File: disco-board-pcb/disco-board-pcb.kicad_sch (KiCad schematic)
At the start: 140 parts, among them J1 Conn_02x32_Odd_Even, J2 Conn_02x32_Odd_Even, U1 MMA8653FCR1

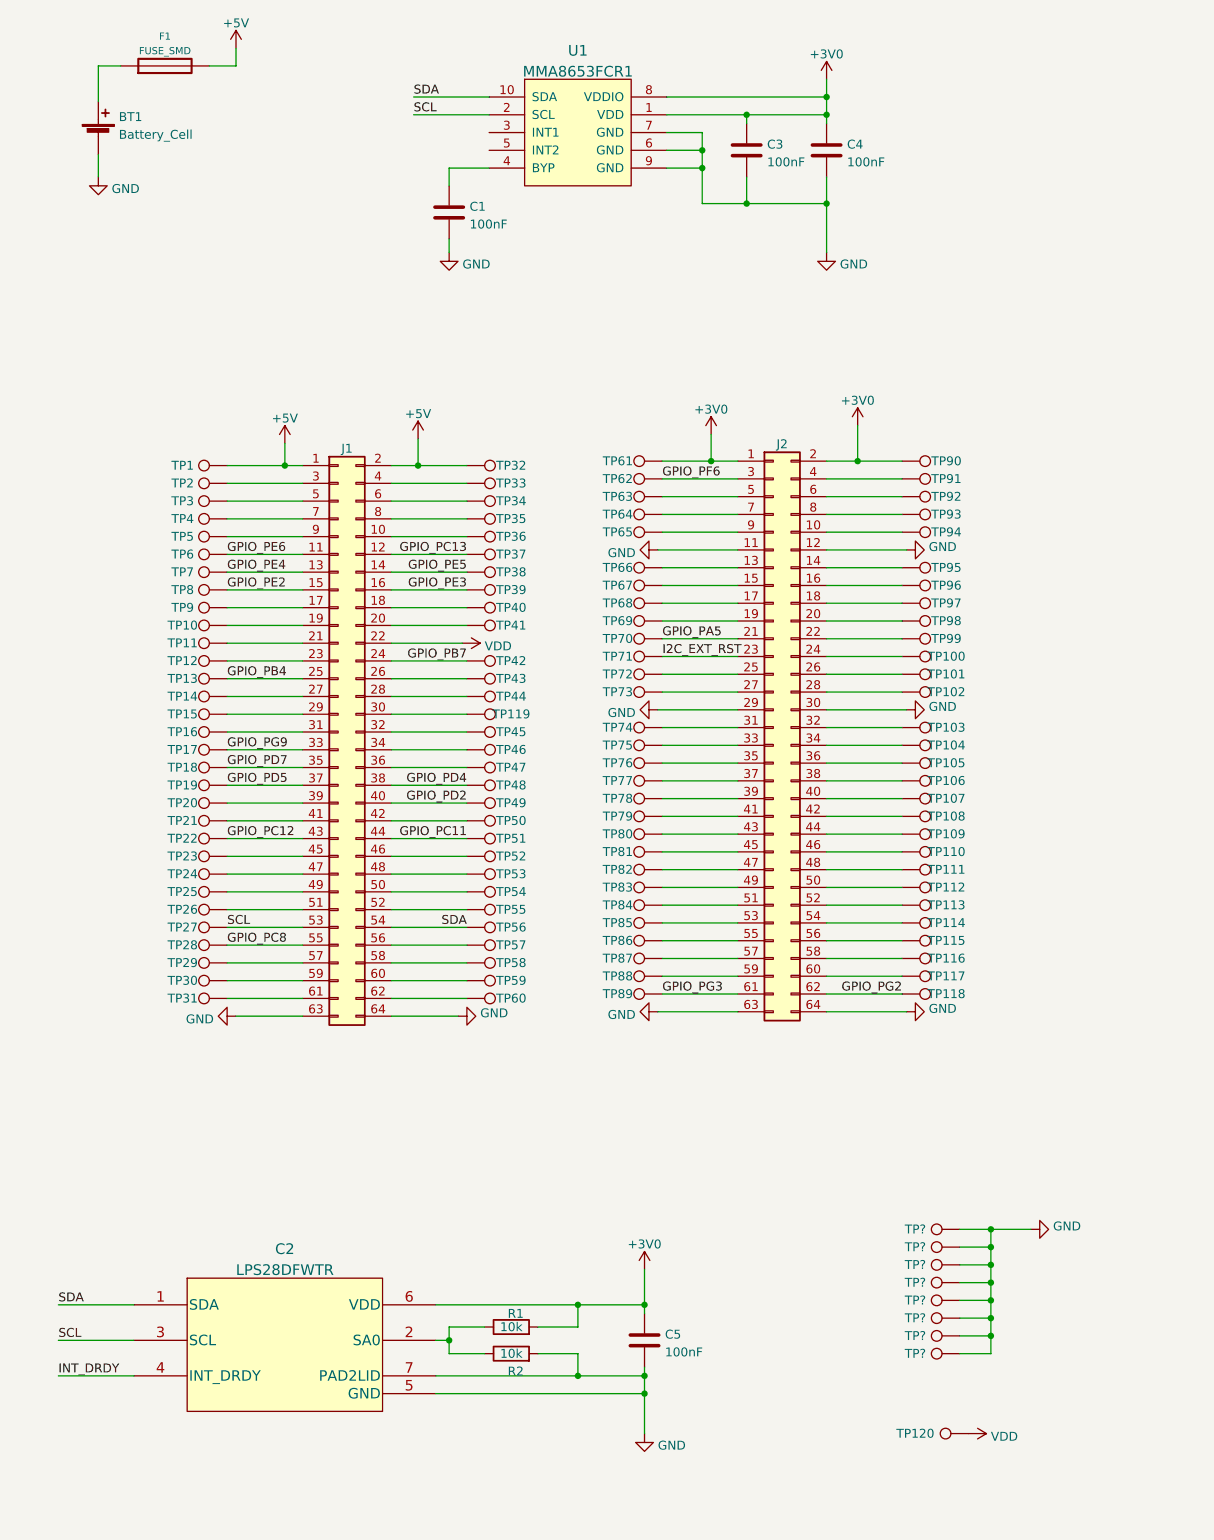
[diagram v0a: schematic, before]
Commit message: Completed routing the board
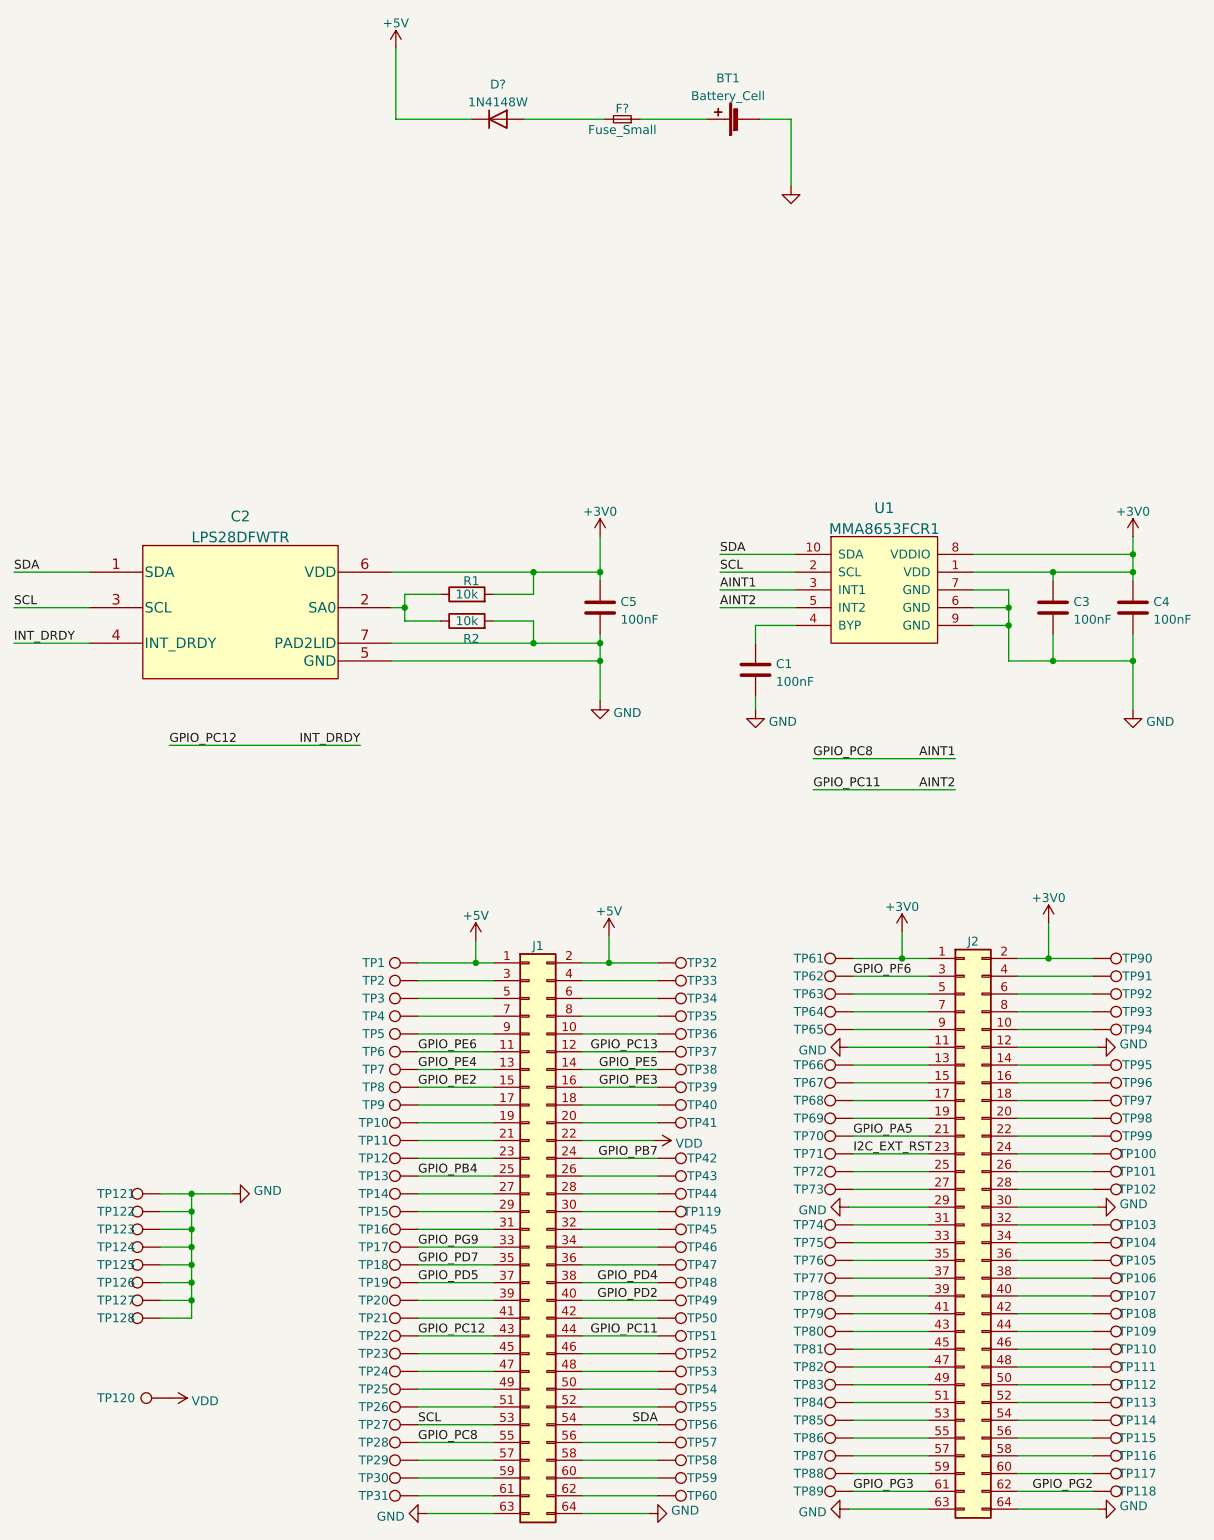
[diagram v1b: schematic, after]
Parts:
- removed F1: FUSE_SMD, Fuse_AKL:Fuse_1206_3216Metric_Pad1.42x1.75mm_BigPads, symbol Special-local:FUSE_SMD
- added D?: 1N4148W, Diode_SMD:D_SOD-123, symbol Diode:1N4148W
- added F?: Fuse_Small, Fuse_AKL:Fuse_1206_3216Metric, symbol magniblu-rescue:Fuse_Small
- gave numbers to parts that had none: 8
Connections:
- net GPIO_PC11 is gone; now on net AINT2: J1.44 (Pin_44), TP51.1
- net GPIO_PC8 is gone; now on net AINT1: J1.55 (Pin_55), TP28.1
- net INT_DRDY is gone; now on net GPIO_PC12: C2.4 (INT_DRDY)
- net +5V: now also D?.1 (K)
- net at BT1.1 (+): now also F?.1
- net AINT1: now reaches U1.3 (INT1)
- net AINT2: now reaches U1.5 (INT2)
- new net: D?.2 (A), F?.2
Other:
- moved on the sheet: BT1, C1, C2, C3, C4, C5, J1, J2, R1, R2, TP1, TP10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

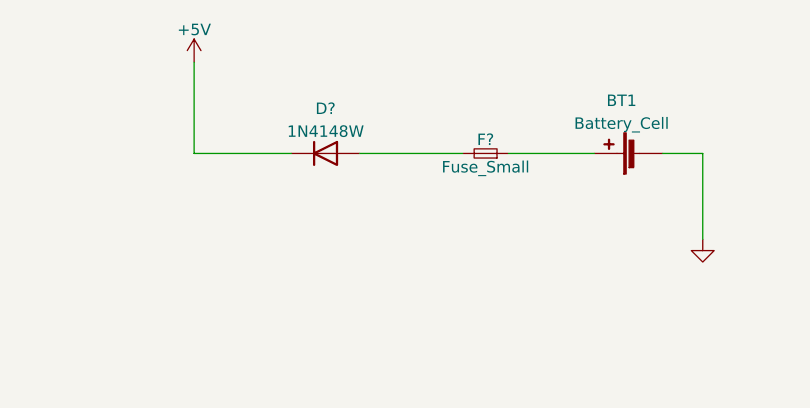
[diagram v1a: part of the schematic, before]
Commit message: Adding gerbers and completing saving schematic
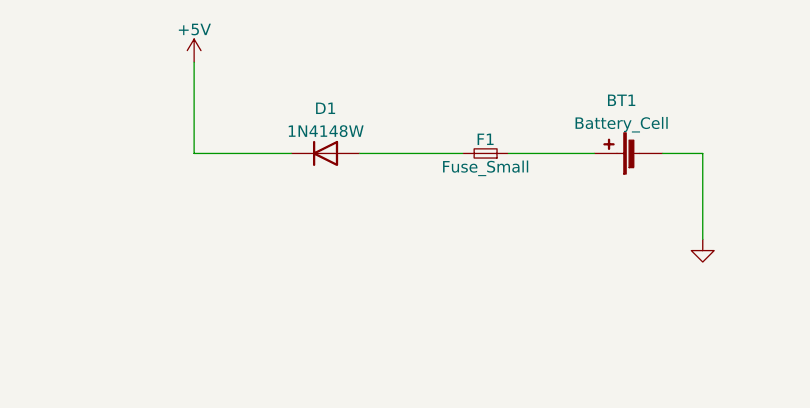
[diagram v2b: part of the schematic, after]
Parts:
- gave numbers to parts that had none: 2
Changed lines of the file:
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@@
   (symbol (lib_id "magniblu-rescue:Fuse_Small") (at 108.585 45.085 180) (unit 1)
     (in_bom yes) (on_board yes)
-    (property "Reference" "F?" (id 0) (at 108.585 43.561 0))
+    (property "Reference" "F1" (id 0) (at 108.585 43.561 0))
     (property "Value" "Fuse_Small" (id 1) (at 108.585 46.609 0))
     (property "Footprint" "Fuse_AKL:Fuse_1206_3216Metric" (id 2) (at 108.585 45.085 0)
@@
   (symbol (lib_id "magniblu-rescue:GND") (at 132.715 54.61 0) (unit 1)
     (in_bom yes) (on_board yes)
-    (property "Reference" "#PWR?" (id 0) (at 132.715 54.61 0)
+    (property "Reference" "#PWR0103" (id 0) (at 132.715 54.61 0)
       (effects (font (size 0.762 0.762)) hide)
     )
@@
   (symbol (lib_id "power:+5V") (at 76.2 34.925 0) (unit 1)
     (in_bom yes) (on_board yes) (fields_autoplaced)
-    (property "Reference" "#PWR?" (id 0) (at 76.2 38.735 0)
+    (property "Reference" "#PWR0102" (id 0) (at 76.2 38.735 0)
       (effects (font (size 1.27 1.27)) hide)
     )
@@
   (symbol (lib_id "Diode:1N4148W") (at 90.805 45.085 0) (unit 1)
     (in_bom yes) (on_board yes) (fields_autoplaced)
-    (property "Reference" "D?" (id 0) (at 90.805 40.1152 0))
+    (property "Reference" "D1" (id 0) (at 90.805 40.1152 0))
     (property "Value" "1N4148W" (id 1) (at 90.805 42.6521 0))
     (property "Footprint" "Diode_SMD:D_SOD-123" (id 2) (at 90.805 49.53 0)
@@
       (reference "#PWR0101") (unit 1) (value "GND") (footprint "")
     )
+    (path "/bdf1c676-962d-47bf-915b-26fdc0ea8afc"
+      (reference "#PWR0102") (unit 1) (value "+5V") (footprint "")
+    )
     (path "/6b5ebafa-a87c-42f6-a5fb-5098cdda5147"
-      (reference "#PWR?") (unit 1) (value "GND") (footprint "")
-    )
-    (path "/bdf1c676-962d-47bf-915b-26fdc0ea8afc"
-      (reference "#PWR?") (unit 1) (value "+5V") (footprint "")
+      (reference "#PWR0103") (unit 1) (value "GND") (footprint "")
     )
     (path "/927ac2c7-5f63-4d17-b9d2-5c71e37a548d"
@@
     )
     (path "/f93f7daa-5ca5-4cea-809d-0241d3212e65"
-      (reference "D?") (unit 1) (value "1N4148W") (footprint "Diode_SMD:D_SOD-123")
+      (reference "D1") (unit 1) (value "1N4148W") (footprint "Diode_SMD:D_SOD-123")
     )
     (path "/3f5c6376-45c6-4e53-a41d-8b01554ee37f"
-      (reference "F?") (unit 1) (value "Fuse_Small") (footprint "Fuse_AKL:Fuse_1206_3216Metric")
+      (reference "F1") (unit 1) (value "Fuse_Small") (footprint "Fuse_AKL:Fuse_1206_3216Metric")
     )
     (path "/4aa4aa55-ca95-4b66-9104-931b593b367e"

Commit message: Adding schematic and images to pcb files
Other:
- title: (none) -> DISCO-F429ZI shield board
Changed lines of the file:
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@@
 (kicad_sch (version 20211123) (generator eeschema)
   (paper "A4" portrait)
+  (title_block
+    (title "DISCO-F429ZI shield board")
+    (date "2022-05-16")
+    (rev "1")
+  )
   (junction (at 105.41 120.015) (diameter 0) (color 0 0 0 0)
   )
